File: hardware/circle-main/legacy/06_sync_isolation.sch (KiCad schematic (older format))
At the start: 5 parts, among them J30 SYNC_IN_BNC, J31 SYNC_OUT_BNC, Q30 SYNC_OUT_OPEN_DRAIN, U30 ISOW7742, U31 TTL_WINDOW_COMPARATOR

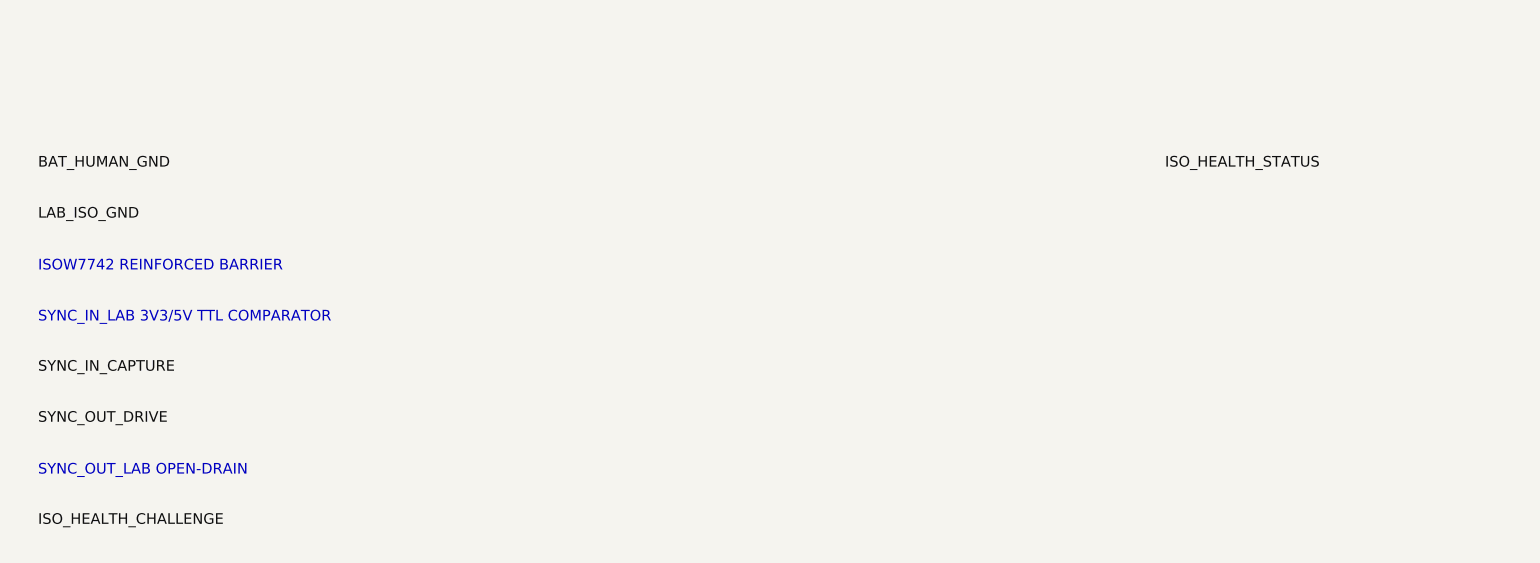
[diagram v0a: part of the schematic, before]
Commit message: Make every CIRCLE review claim reproducible
Validate and export the architecture-level schematics with KiCad 10.0.5, add zero-violation ERC gates, engineering documentation, and one-command evidence hashing.

Constraint: KiCad CLI does not import legacy .sch into native .kicad_sch

Rejected: Hand-written native S-expressions | would create unvalidated CAD

Confidence: medium

Scope-risk: broad

Reversibility: clean

Directive: Treat NET annotations as architecture interfaces, not fabrication-ready connectivity

Tested: py -3.11 tools/verify_release.py; 30 tests; KiCad 10.0.5 ERC/BOM/PDF/SVG/netlist exports

Not-tested: Native conversion, PCB layout, footprints, powered electrodes, human connection, EMC, or regulatory compliance
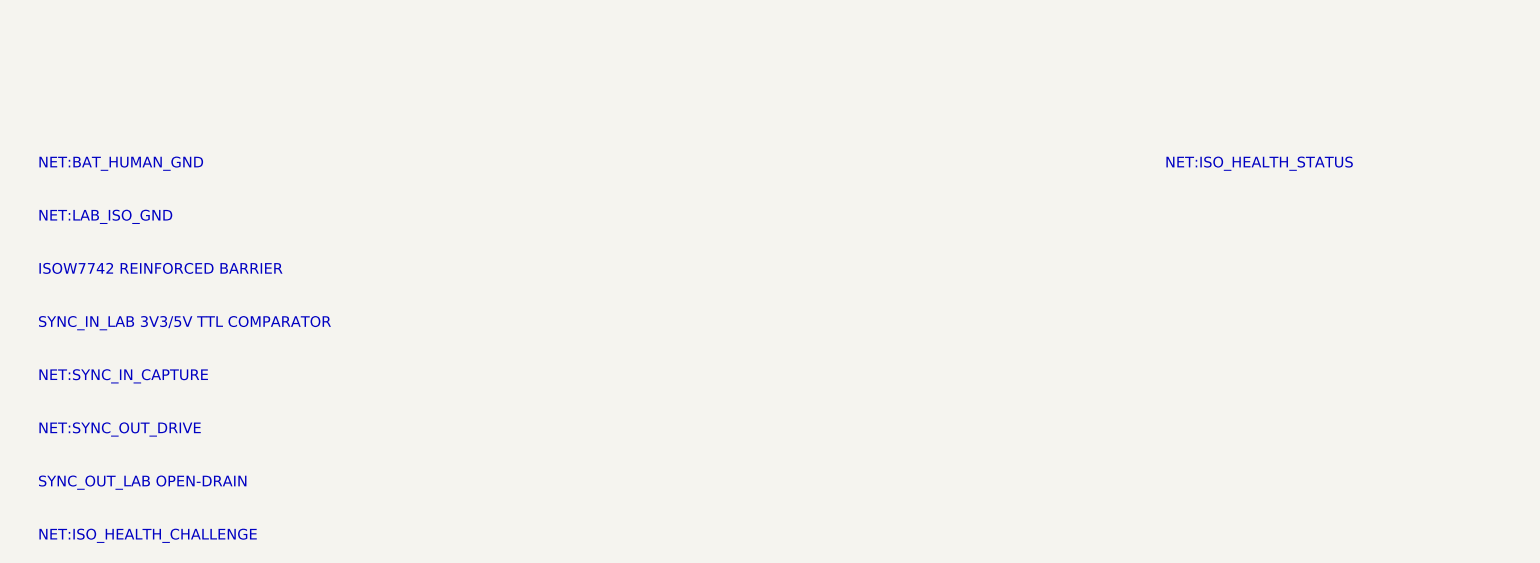
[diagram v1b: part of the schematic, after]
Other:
- note added: "NET:BAT_HUMAN_GND"
- note added: "NET:ISO_HEALTH_CHALLENGE"
- note added: "NET:ISO_HEALTH_STATUS"
- note added: "NET:LAB_ISO_GND"
- note added: "NET:SYNC_IN_CAPTURE"
- note added: "NET:SYNC_OUT_DRIVE"
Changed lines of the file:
@@
 Sheet 1 1
 Title "Isolated SYNC IN and OUT"
+Date "2026-08-14"
+Rev "A"
+Comp "Vers3Dynamics"
 Comment1 "ENGINEERING REVIEW ONLY - NOT FOR HUMAN CONNECTION"
+Comment2 "Generated artifact - edit manifest/generator"
+Comment3 ""
+Comment4 ""
 $EndDescr
 $Comp
@@
 F 0 "U30" H 1400 1300 50  0000 C CNN
 F 1 "ISOW7742" H 1400 1100 50  0000 C CNN
+F 2 "" H 1300 1200 50  0001 C CNN
+F 3 "" H 1300 1200 50  0001 C CNN
+	1    1300 1200
 	1    0    0    -1
 $EndComp
@@
 F 0 "U31" H 3500 1300 50  0000 C CNN
 F 1 "TTL_WINDOW_COMPARATOR" H 3500 1100 50  0000 C CNN
+F 2 "" H 3400 1200 50  0001 C CNN
+F 3 "" H 3400 1200 50  0001 C CNN
+	1    3400 1200
 	1    0    0    -1
 $EndComp
@@
 F 0 "Q30" H 5600 1300 50  0000 C CNN
 F 1 "SYNC_OUT_OPEN_DRAIN" H 5600 1100 50  0000 C CNN
+F 2 "" H 5500 1200 50  0001 C CNN
+F 3 "" H 5500 1200 50  0001 C CNN
+	1    5500 1200
 	1    0    0    -1
 $EndComp
@@
 F 0 "J30" H 7700 1300 50  0000 C CNN
 F 1 "SYNC_IN_BNC" H 7700 1100 50  0000 C CNN
+F 2 "" H 7600 1200 50  0001 C CNN
+F 3 "" H 7600 1200 50  0001 C CNN
+	1    7600 1200
 	1    0    0    -1
 $EndComp
@@
 F 0 "J31" H 1400 2100 50  0000 C CNN
 F 1 "SYNC_OUT_BNC" H 1400 1900 50  0000 C CNN
+F 2 "" H 1300 2000 50  0001 C CNN
+F 3 "" H 1300 2000 50  0001 C CNN
+	1    1300 2000
 	1    0    0    -1
 $EndComp
-Text Label 700 5600 0    50   ~ 0
-BAT_HUMAN_GND
-Text Label 700 5840 0    50   ~ 0
-LAB_ISO_GND
-Text Label 700 6560 0    50   ~ 0
-SYNC_IN_CAPTURE
-Text Label 700 6800 0    50   ~ 0
-SYNC_OUT_DRIVE
-Text Label 700 7280 0    50   ~ 0
-ISO_HEALTH_CHALLENGE
-Text Label 6000 5600 0    50   ~ 0
-ISO_HEALTH_STATUS
 Text Notes 600 400 0    50   ~ 0
 ENGINEERING REVIEW ONLY - NOT FOR HUMAN CONNECTION
-Text Notes 700 6080 0    50   ~ 0
+Text Notes 700 5600 0    50   ~ 0
+NET:BAT_HUMAN_GND
+Text Notes 700 5850 0    50   ~ 0
+NET:LAB_ISO_GND
+Text Notes 700 6100 0    50   ~ 0
 ISOW7742 REINFORCED BARRIER
-Text Notes 700 6320 0    50   ~ 0
+Text Notes 700 6350 0    50   ~ 0
 SYNC_IN_LAB 3V3/5V TTL COMPARATOR
-Text Notes 700 7040 0    50   ~ 0
+Text Notes 700 6600 0    50   ~ 0
+NET:SYNC_IN_CAPTURE
+Text Notes 700 6850 0    50   ~ 0
+NET:SYNC_OUT_DRIVE
+Text Notes 700 7100 0    50   ~ 0
 SYNC_OUT_LAB OPEN-DRAIN
+Text Notes 700 7350 0    50   ~ 0
+NET:ISO_HEALTH_CHALLENGE
+Text Notes 6000 5600 0    50   ~ 0
+NET:ISO_HEALTH_STATUS
 $EndSCHEMATC
